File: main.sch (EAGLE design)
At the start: 1 part

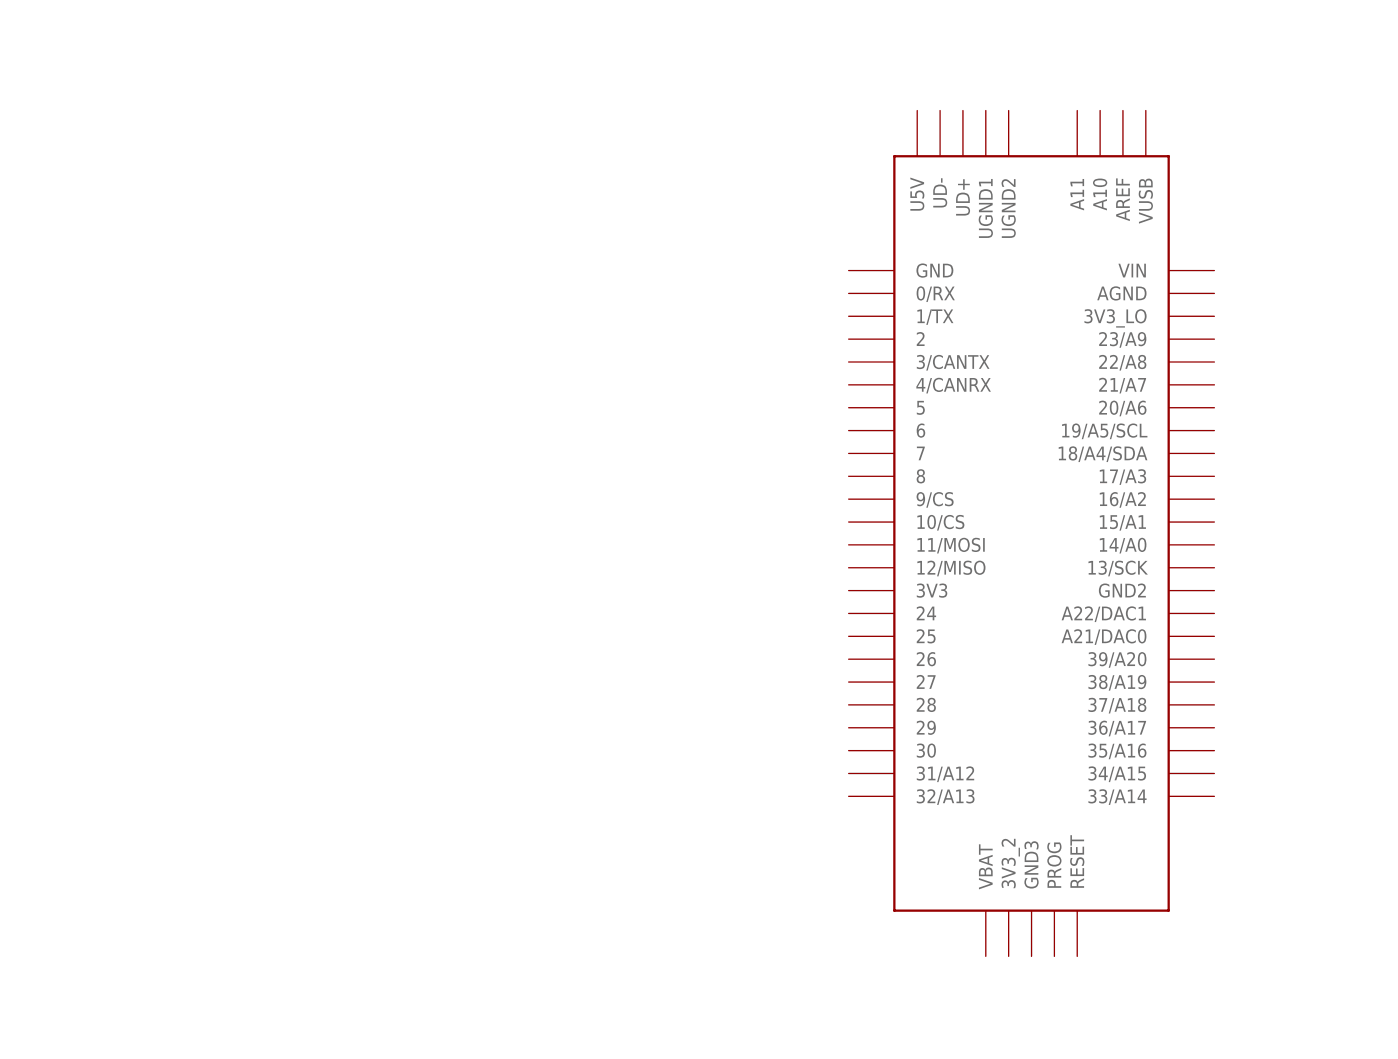
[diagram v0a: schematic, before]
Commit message: main update and unused restructured
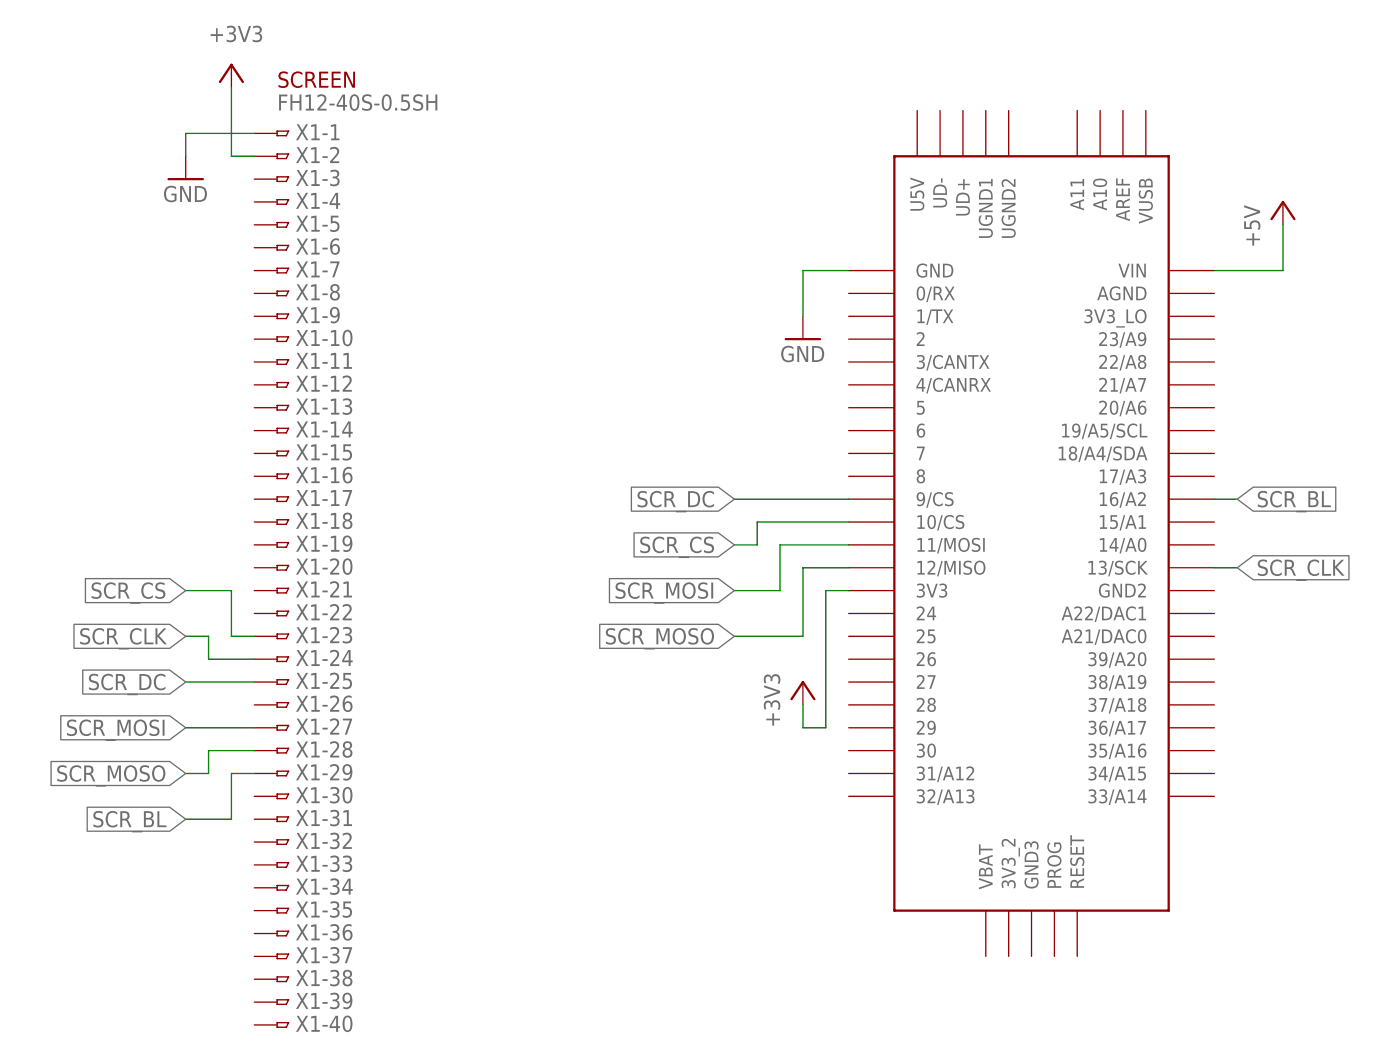
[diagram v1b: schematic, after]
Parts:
- added X1: FH12-40S-0.5SH, con-hirose:FH12-40S-0.5SH
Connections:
- new net +3V3: U$1.3V3, X1-2.1
- new net +5V: U$1.VIN
- new net GND: U$1.GND, X1-1.1
- new net SCR_BL: U$1.16/A2, X1-29.1
- new net SCR_CLK: U$1.13/SCK, X1-24.1
- new net SCR_CS: U$1.10/CS, X1-23.1
- new net SCR_DC: U$1.9/CS, X1-25.1
- new net SCR_MOSI: U$1.11/MOSI, X1-27.1
- new net SCR_MOSO: U$1.12/MISO, X1-28.1
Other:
- note added: "SCREEN"

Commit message: milestone all connectors sch TODO routing and expansion
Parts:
- added AUDIO: (no value), pinhead:PINHD-1X3
- added BUTTONS, SOUND_MODULES_EXPANSION: (no value), pinhead:PINHD-2X4
- added GENERAL_EXPANSION: (no value), pinhead:PINHD-2X5
- added KNOBBOARD: (no value), con-dil:IC14PL
- added PORTBOARD: (no value), con-dil:IC24PL
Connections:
- new net AUDIO_GND: AUDIO.2, U$1.AGND
- new net AUDIO_L: AUDIO.3, U$1.A21/DAC0
- new net AUDIO_R: AUDIO.1, U$1.A22/DAC1
- new net JOYSTICK_B: KNOBBOARD.8
- new net JOYSTICK_X: KNOBBOARD.6
- new net JOYSTICK_Y: KNOBBOARD.7
- new net N$10: PORTBOARD.20
- new net N$11: PORTBOARD.19
- new net N$12: PORTBOARD.18
- new net N$3: PORTBOARD.3
- new net N$4: PORTBOARD.4
- new net N$5: PORTBOARD.5
- new net N$6: PORTBOARD.6
- new net N$7: PORTBOARD.7
- new net N$8: PORTBOARD.22
- new net N$9: PORTBOARD.21
- new net ROTENC1_A: KNOBBOARD.2
- new net ROTENC1_B: KNOBBOARD.3
- new net ROTENC2_A: KNOBBOARD.4
- new net ROTENC2_B: KNOBBOARD.5
- new net ROTENC3_A: KNOBBOARD.13
- new net ROTENC3_B: KNOBBOARD.12
- new net ROTENC4_A: KNOBBOARD.11
- new net ROTENC4_B: KNOBBOARD.10
- net +3V3: now also KNOBBOARD.1, PORTBOARD.24
- net +5V: now also PORTBOARD.23
- net GND: now also KNOBBOARD.14, PORTBOARD.1, PORTBOARD.2
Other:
- moved on the sheet: X1-1, X1-10, X1-11, X1-12, X1-13, X1-14, X1-15, X1-16, X1-17, X1-18, X1-19, X1-2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

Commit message: pcb cleanup and audio_main tidy
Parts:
- removed AUDIO: (no value), pinhead:PINHD-1X3
- added AUDIO_MAIN: (no value), pinhead:PINHD-1X3
- renumbered GENERAL_EXPANSION to GENERAL_XPN, SOUND_MODULES_EXPANSION to SOUND_MOD_XPN
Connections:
- net AUDIO_GND: now also AUDIO_MAIN.2; no longer AUDIO.2
- net AUDIO_L: now also AUDIO_MAIN.1; no longer AUDIO.3
- net AUDIO_R: now also AUDIO_MAIN.3; no longer AUDIO.1
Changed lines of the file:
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@@
 <part name="+3V3" library="supply1" library_urn="urn:adsk.eagle:library:371" deviceset="+3V3" device=""/>
 <part name="GND3" library="supply1" library_urn="urn:adsk.eagle:library:371" deviceset="GND" device=""/>
-<part name="AUDIO" library="pinhead" library_urn="urn:adsk.eagle:library:325" deviceset="PINHD-1X3" device="" package3d_urn="urn:adsk.eagle:package:22458/2"/>
 <part name="KNOBBOARD" library="con-dil" library_urn="urn:adsk.eagle:library:140" deviceset="IC14PL" device="" package3d_urn="urn:adsk.eagle:package:6625/1"/>
 <part name="PORTBOARD" library="con-dil" library_urn="urn:adsk.eagle:library:140" deviceset="IC24PL" device="" package3d_urn="urn:adsk.eagle:package:6627/1"/>
@@
 <part name="P+2" library="supply1" library_urn="urn:adsk.eagle:library:371" deviceset="+5V" device=""/>
 <part name="+3V4" library="supply1" library_urn="urn:adsk.eagle:library:371" deviceset="+3V3" device=""/>
-<part name="GENERAL_EXPANSION" library="pinhead" library_urn="urn:adsk.eagle:library:325" deviceset="PINHD-2X5" device="" package3d_urn="urn:adsk.eagle:package:22470/2"/>
+<part name="GENERAL_XPN" library="pinhead" library_urn="urn:adsk.eagle:library:325" deviceset="PINHD-2X5" device="" package3d_urn="urn:adsk.eagle:package:22470/2"/>
 <part name="BUTTONS" library="pinhead" library_urn="urn:adsk.eagle:library:325" deviceset="PINHD-2X4" device="" package3d_urn="urn:adsk.eagle:package:22461/2"/>
-<part name="SOUND_MODULES_EXPANSION" library="pinhead" library_urn="urn:adsk.eagle:library:325" deviceset="PINHD-2X4" device="" package3d_urn="urn:adsk.eagle:package:22461/2"/>
+<part name="SOUND_MOD_XPN" library="pinhead" library_urn="urn:adsk.eagle:library:325" deviceset="PINHD-2X4" device="" package3d_urn="urn:adsk.eagle:package:22461/2"/>
+<part name="AUDIO_MAIN" library="pinhead" library_urn="urn:adsk.eagle:library:325" deviceset="PINHD-1X3" device="" package3d_urn="urn:adsk.eagle:package:22458/2"/>
 </parts>
 <sheets>
@@
 <attribute name="VALUE" x="-92.71" y="119.126" size="1.778" layer="96" rot="R180"/>
 </instance>
-<instance part="AUDIO" gate="A" x="-5.08" y="12.7" smashed="yes">
-<attribute name="NAME" x="-11.43" y="18.415" size="1.778" layer="95"/>
-<attribute name="VALUE" x="-11.43" y="5.08" size="1.778" layer="96"/>
-</instance>
 <instance part="KNOBBOARD" gate="1" x="-111.76" y="104.14" smashed="yes">
 <attribute name="VALUE" x="-115.57" y="91.44" size="1.778" layer="96"/>
@@
 <attribute name="VALUE" x="-45.72" y="124.46" size="1.778" layer="96" rot="R90"/>
 </instance>
-<instance part="GENERAL_EXPANSION" gate="A" x="-17.78" y="76.2" smashed="yes">
+<instance part="GENERAL_XPN" gate="A" x="-17.78" y="76.2" smashed="yes">
 <attribute name="NAME" x="-24.13" y="84.455" size="1.778" layer="95"/>
 <attribute name="VALUE" x="-24.13" y="66.04" size="1.778" layer="96"/>
@@
 <attribute name="VALUE" x="-24.13" y="93.98" size="1.778" layer="96"/>
 </instance>
-<instance part="SOUND_MODULES_EXPANSION" gate="A" x="7.62" y="101.6" smashed="yes">
+<instance part="SOUND_MOD_XPN" gate="A" x="7.62" y="101.6" smashed="yes">
 <attribute name="NAME" x="1.27" y="109.855" size="1.778" layer="95"/>
 <attribute name="VALUE" x="1.27" y="93.98" size="1.778" layer="96"/>
+</instance>
+<instance part="AUDIO_MAIN" gate="A" x="17.78" y="76.2" smashed="yes">
+<attribute name="NAME" x="11.43" y="81.915" size="1.778" layer="95"/>
+<attribute name="VALUE" x="11.43" y="68.58" size="1.778" layer="96"/>
 </instance>
 </instances>
@@
 <segment>
 <pinref part="U$1" gate="G$1" pin="A22/DAC1"/>
-<pinref part="AUDIO" gate="A" pin="1"/>
-<wire x1="-35.56" y1="15.24" x2="-7.62" y2="15.24" width="0.1524" layer="91"/>
-<label x="-20.32" y="15.24" size="1.27" layer="95" rot="R90" xref="yes"/>
+<wire x1="-35.56" y1="15.24" x2="-33.02" y2="15.24" width="0.1524" layer="91"/>
+<label x="-33.02" y="15.24" size="1.27" layer="95" xref="yes"/>
+</segment>
+<segment>
+<pinref part="AUDIO_MAIN" gate="A" pin="3"/>
+<wire x1="15.24" y1="73.66" x2="10.16" y2="73.66" width="0.1524" layer="91"/>
+<label x="10.16" y="73.66" size="1.27" layer="95" rot="R180" xref="yes"/>
 </segment>
 </net>
@@
 <segment>
 <pinref part="U$1" gate="G$1" pin="A21/DAC0"/>
-<wire x1="-35.56" y1="12.7" x2="-30.48" y2="12.7" width="0.1524" layer="91"/>
-<wire x1="-30.48" y1="12.7" x2="-30.48" y2="10.16" width="0.1524" layer="91"/>
-<pinref part="AUDIO" gate="A" pin="3"/>
-<wire x1="-30.48" y1="10.16" x2="-7.62" y2="10.16" width="0.1524" layer="91"/>
-<label x="-20.32" y="10.16" size="1.27" layer="95" rot="R270" xref="yes"/>
+<wire x1="-35.56" y1="12.7" x2="-33.02" y2="12.7" width="0.1524" layer="91"/>
+<label x="-33.02" y="12.7" size="1.27" layer="95" xref="yes"/>
+</segment>
+<segment>
+<pinref part="AUDIO_MAIN" gate="A" pin="1"/>
+<wire x1="15.24" y1="78.74" x2="10.16" y2="78.74" width="0.1524" layer="91"/>
+<label x="10.16" y="78.74" size="1.27" layer="95" rot="R180" xref="yes"/>
 </segment>
 </net>
@@
 </segment>
 <segment>
-<pinref part="AUDIO" gate="A" pin="2"/>
-<wire x1="-7.62" y1="12.7" x2="-15.24" y2="12.7" width="0.1524" layer="91"/>
-<label x="-15.24" y="12.7" size="1.27" layer="95" rot="R180" xref="yes"/>
-</segment>
-</net>
+<pinref part="AUDIO_MAIN" gate="A" pin="2"/>
+<wire x1="15.24" y1="76.2" x2="10.16" y2="76.2" width="0.1524" layer="91"/>
+<label x="10.16" y="76.2" size="1.27" layer="95" rot="R180" xref="yes"/>
+</segment>
+</net>

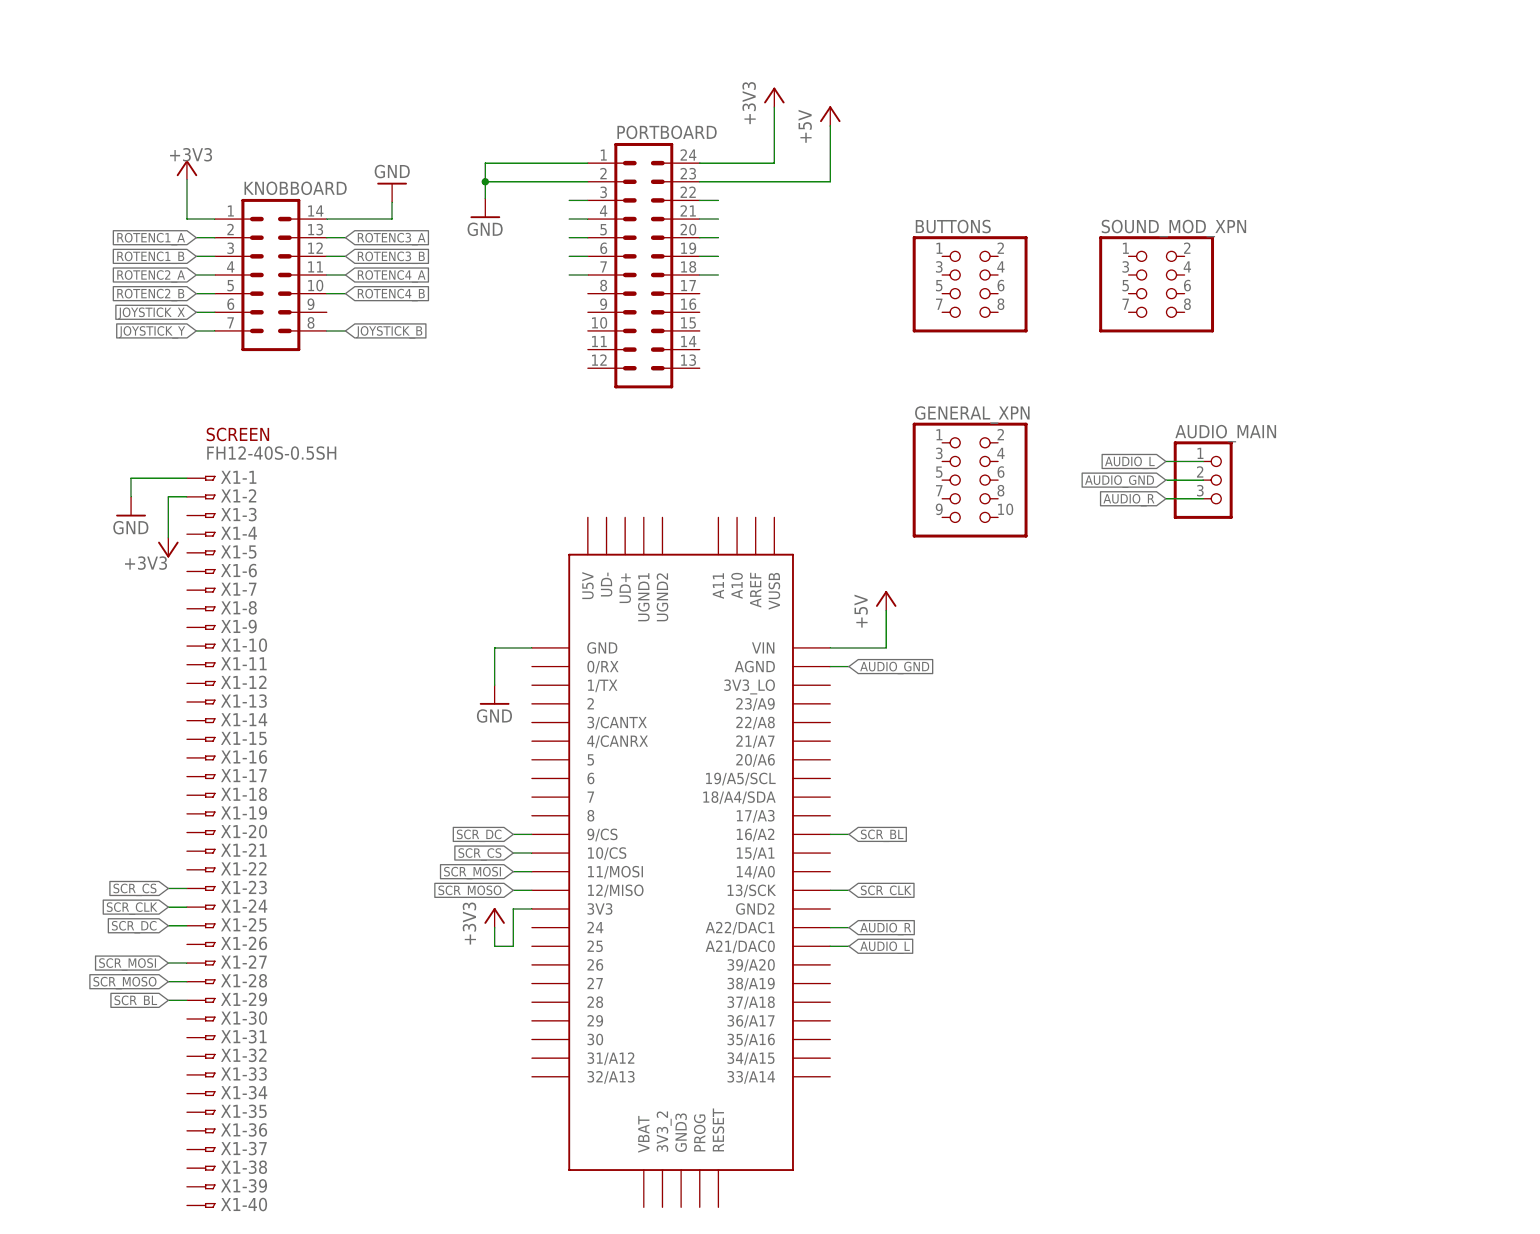
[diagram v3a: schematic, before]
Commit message: general expansion slots
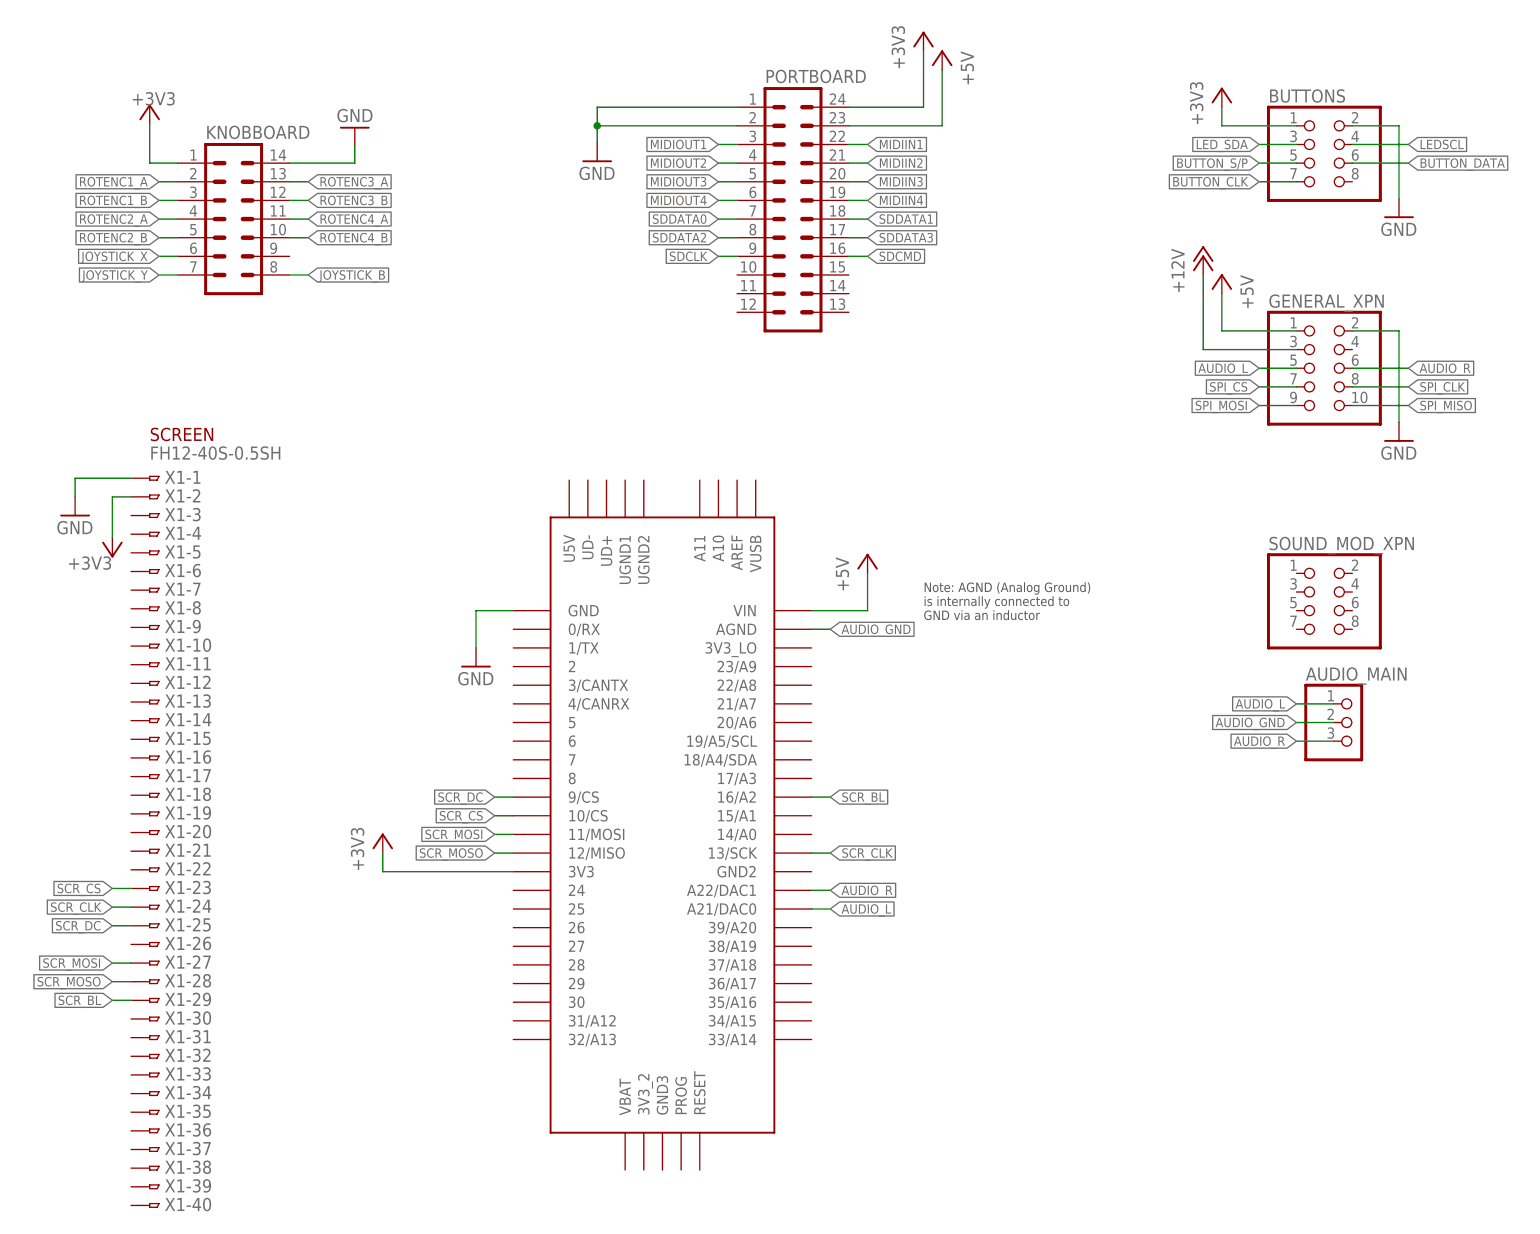
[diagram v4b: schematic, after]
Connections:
- net N$10 renamed MIDIIN3
- net N$11 renamed MIDIIN4
- net N$12 renamed SDDATA1
- net N$3 renamed MIDIOUT1
- net N$4 renamed MIDIOUT2
- net N$5 renamed MIDIOUT3
- net N$6 renamed MIDIOUT4
- net N$7 renamed SDDATA0
- net N$8 renamed MIDIIN1
- net N$9 renamed MIDIIN2
- new net +12V: GENERAL_XPN.3
- new net BUTTON_CLK: BUTTONS.7
- new net BUTTON_DATA: BUTTONS.6
- new net BUTTON_S/P: BUTTONS.5
- new net LEDSCL: BUTTONS.4
- new net LED_SDA: BUTTONS.3
- new net SDCLK: PORTBOARD.9
- new net SDCMD: PORTBOARD.16
- new net SDDATA2: PORTBOARD.8
- new net SDDATA3: PORTBOARD.17
- new net SPI_CLK: GENERAL_XPN.8
- new net SPI_CS: GENERAL_XPN.7
- new net SPI_MISO: GENERAL_XPN.10
- new net SPI_MOSI: GENERAL_XPN.9
- net +3V3: now also BUTTONS.1
- net +5V: now also GENERAL_XPN.1
- net AUDIO_L: now also GENERAL_XPN.5
- net AUDIO_R: now also GENERAL_XPN.6
- net GND: now also BUTTONS.2, GENERAL_XPN.2
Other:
- note added: "Note: AGND (Analog Ground) is internally connected to GND via an inductor"
- moved on the sheet: AUDIO_MAIN, BUTTONS, GENERAL_XPN, KNOBBOARD, PORTBOARD, SOUND_MOD_XPN, X1-1, X1-10, X1-11, X1-12, X1-13, X1-14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
